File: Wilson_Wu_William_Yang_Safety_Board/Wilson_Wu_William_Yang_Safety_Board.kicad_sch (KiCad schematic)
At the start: 0 parts

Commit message: added can
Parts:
- added J1: 22035035, SMV_Connectors:3pin_CON_22035035_MOL, symbol SMV_Custom:3-pin Mini Molex Spox
- added J2: XT60-M, SMV_Connectors:AMASS_XT60-M, symbol SMV_Custom:XT60-M
- added U1: ~, symbol SMV_Custom:STM32_Nucleo_F446RE
- added U2: MCP2562-E/P, PDIP8_300MC_MCH, symbol can-tranciever:MCP2562-E_P

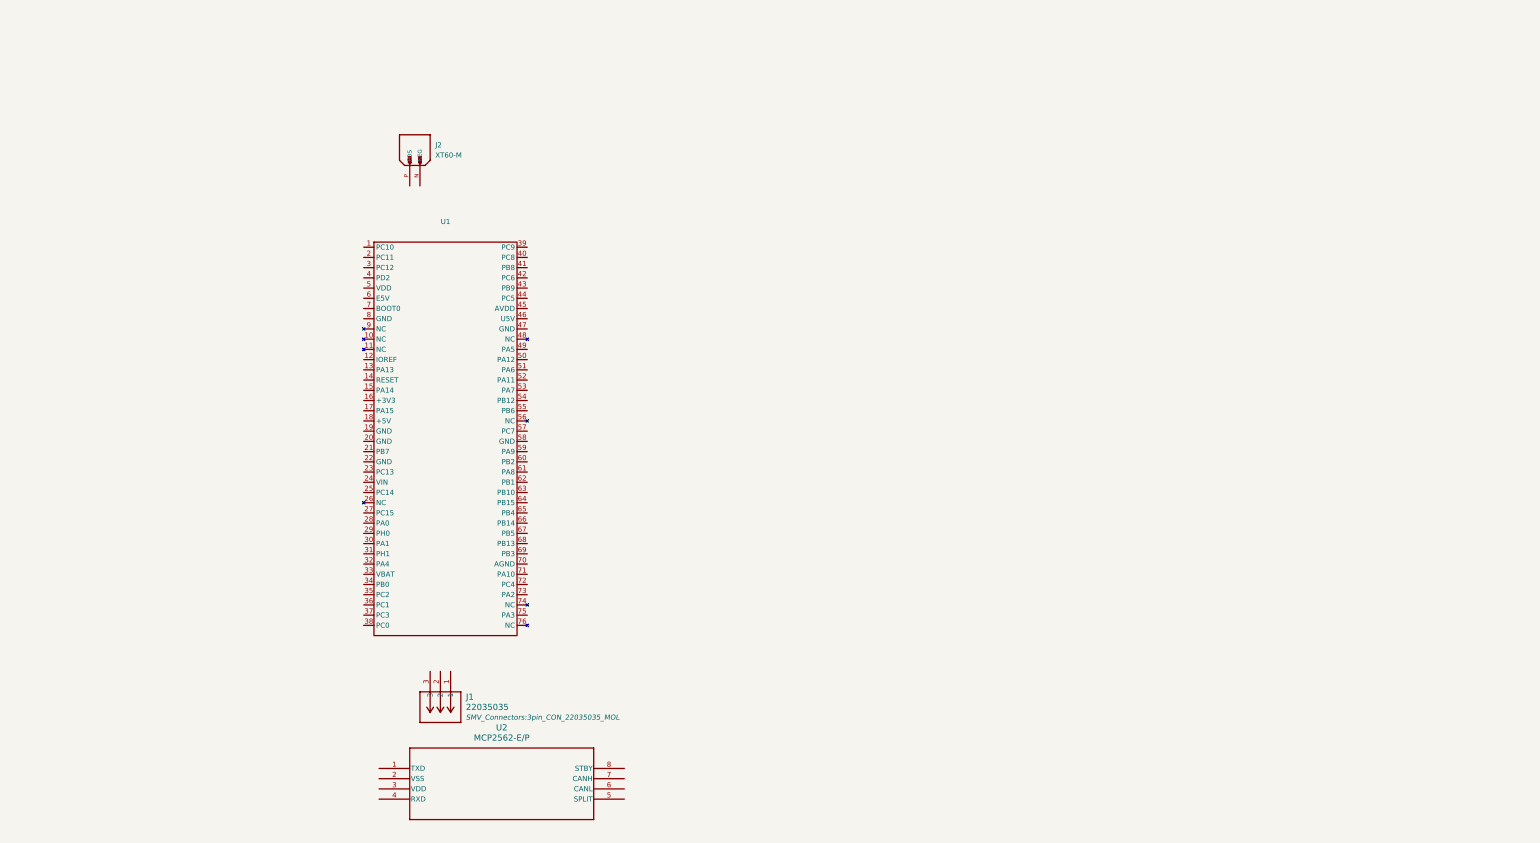
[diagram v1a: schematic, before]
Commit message: added can and power out stuff
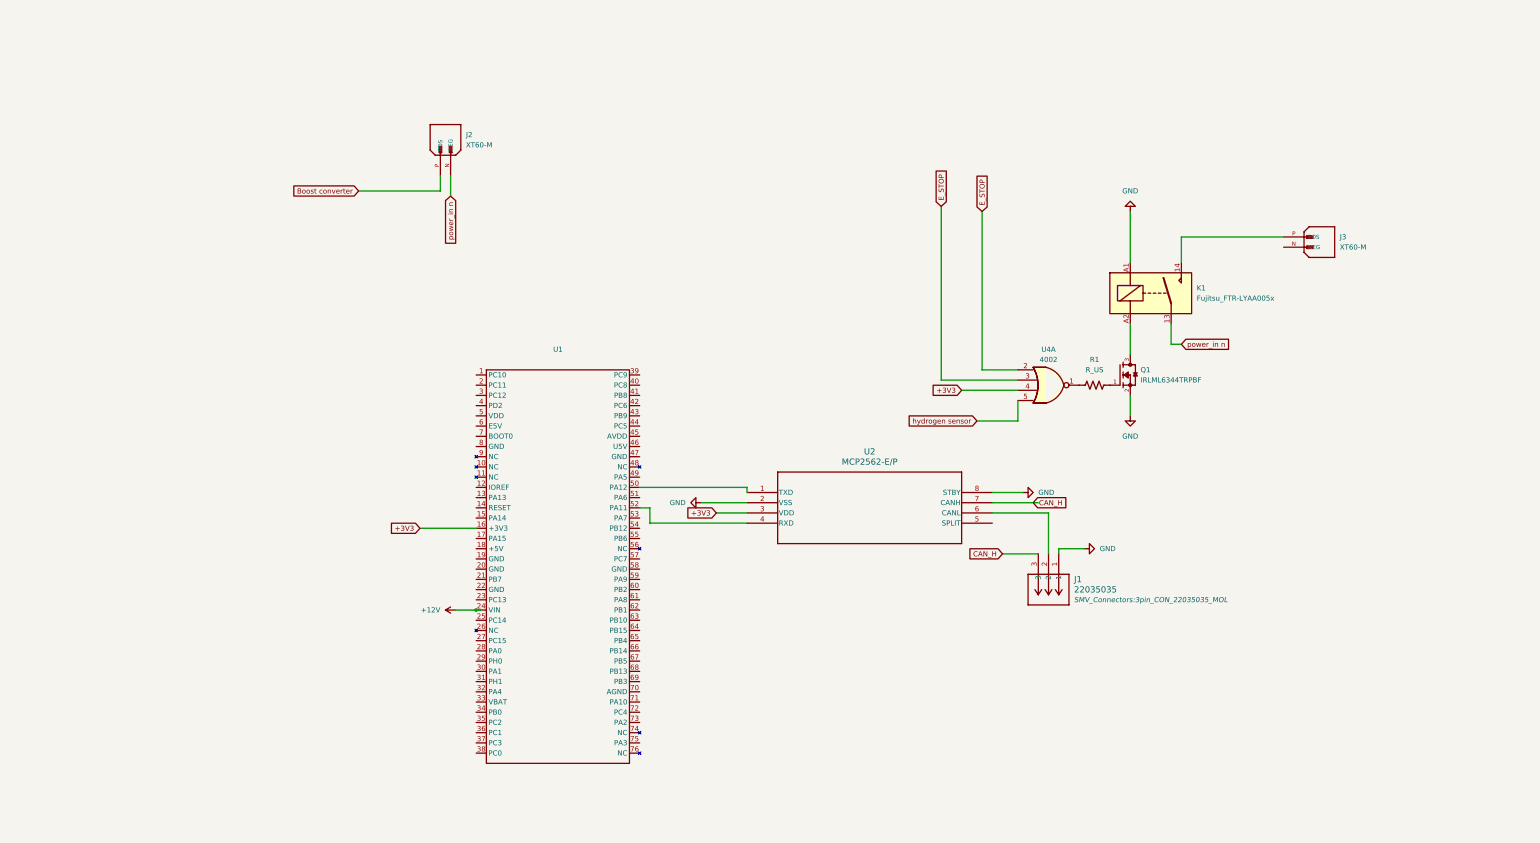
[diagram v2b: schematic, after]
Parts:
- added J3: XT60-M, SMV_Connectors:AMASS_XT60-M, symbol SMV_Custom:XT60-M
- added K1: Fujitsu_FTR-LYAA005x, Relay_THT:Relay_SPST-NO_Fujitsu_FTR-LYAA005x_FormA_Vertical, symbol Relay:Fujitsu_FTR-LYAA005x
- added Q1: IRLML6344TRPBF, IRLML6344TRPBF:TRANS_IRLML6344TRPBF, symbol IRLML6344TRPBF:IRLML6344TRPBF
- added R1: R_US, symbol Device:R_US
- added U4: 4002, symbol 4xxx:4002
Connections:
- net at U2.1 (TXD): now also U1.50 (PA12)
- net GND: now reaches U2.2 (VSS)
- net GND: now also J1.1, U2.8 (STBY), K1.A1, Q1.2
- net +3V3: now reaches U2.3 (VDD)
- net +3V3: now also U1.16 (+3V3), U4.4
- net at U2.4 (RXD): now also U1.52 (PA11)
- net at U2.6 (CANL): now also J1.2
- net CAN_H: now reaches U2.7 (CANH)
- net CAN_H: now also J1.3
- net +12V: now reaches U1.24 (VIN)
- net power_in n: now reaches J2.N (NEG)
- net power_in n: now also K1.13
- net Boost converter: now reaches J2.P (POS)
- new net: J3.P (POS), K1.14
- new net: K1.A2, Q1.3
- new net: R1.1, U4.1
- new net: Q1.1, R1.2
- new net E_STOP: U4.2, U4.3
- new net hydrogen sensor: U4.5
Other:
- moved on the sheet: J1, J2, U1, U2

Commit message: redo
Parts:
- added J4: M22-7130442, M22-7130442_TYC, symbol SMV_Custom:M22-7130442
- added J5: 22035035, SMV_Connectors:3pin_CON_22035035_MOL, symbol SMV_Custom:3-pin Mini Molex Spox
- added J6, J7: 430450200, SMV_Connectors:CONN_SD-43045-001_02_MOL, symbol SMV_Custom:430450200
- added U3: MCP6286T-E/OT, SMV_ICs:SOT-23-5_MC_MCH, symbol SMV_Custom:MCP6286T-E_OT
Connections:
- net GND: now also J5.2, J6.2, J7.2, U3.2 (VSS)
- net at U1.50 (PA12), U2.1 (TXD): now also J4.A1, J4.A4
- net at U1.52 (PA11), U2.4 (RXD): now also J4.A2, J4.A3
- net E_STOP: no longer names the net of U4.2
- net E_STOP: now also J6.1; no longer U4.3
- net hydrogen sensor: no longer names the net of U4.5
- net hydrogen sensor: now also U3.1 (VOUT)
- new net: J7.1, U4.3
- new net +3.3V: J5.1, U3.5 (VDD)
- new net Bridge Circuit: J5.3, U3.3 (VIN+)
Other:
- moved on the sheet: J1, U1, U2

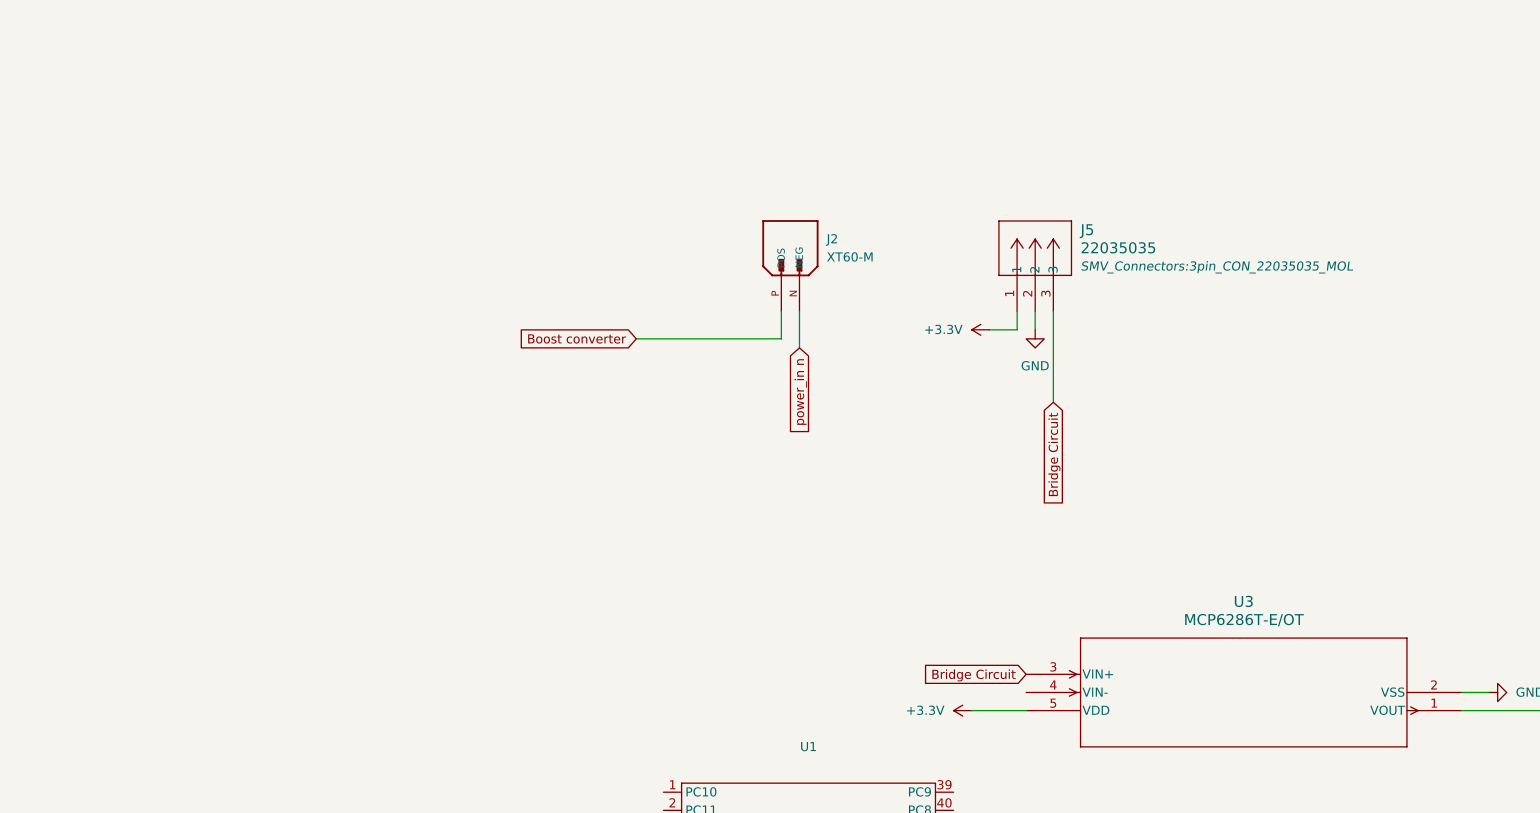
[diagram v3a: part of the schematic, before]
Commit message: added bridge circuit
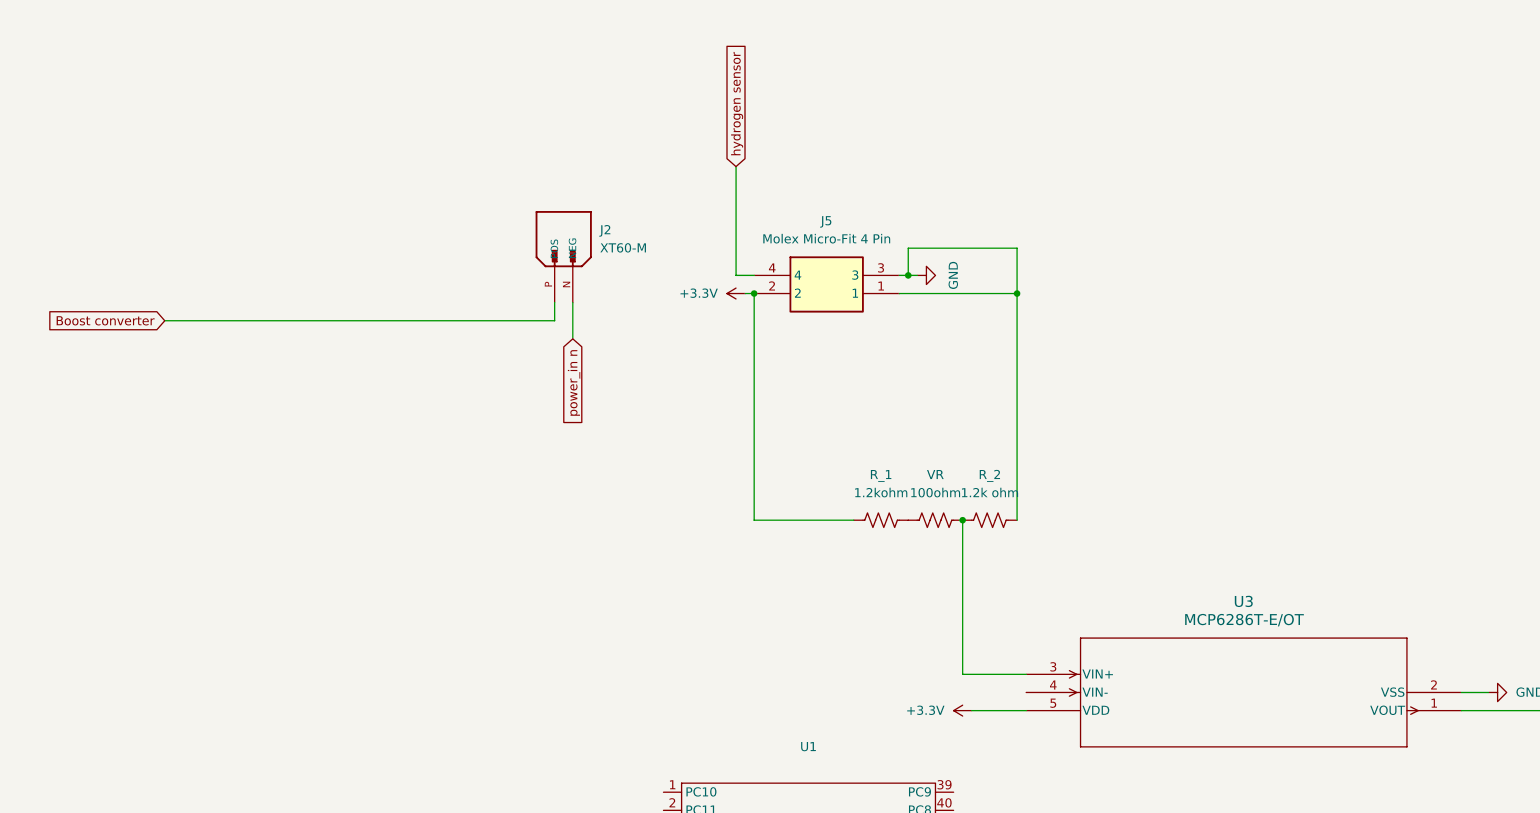
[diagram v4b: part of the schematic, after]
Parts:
- removed J5: 22035035, SMV_Connectors:3pin_CON_22035035_MOL, symbol SMV_Custom:3-pin Mini Molex Spox
- added J5: Molex Micro-Fit 4 Pin, SMV_Connectors:4_pin0430450401, symbol SMV_Custom:Molex Micro-Fit 4 Pin
- added R_1: 1.2kohm, symbol Device:R_US
- added R_2: 1.2k ohm, symbol Device:R_US
- added VR: 100ohm, symbol Device:R_US
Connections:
- net +3.3V: now also J5.2, R_1.1
- net GND: now also J5.1, J5.3, R_2.2
- net Bridge Circuit: no longer names the net of U3.3 (VIN+)
- net Bridge Circuit: now also R_2.1, VR.2
- new net: R_1.2, VR.1
- new net hydrogen sensor: J5.4
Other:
- moved on the sheet: J2

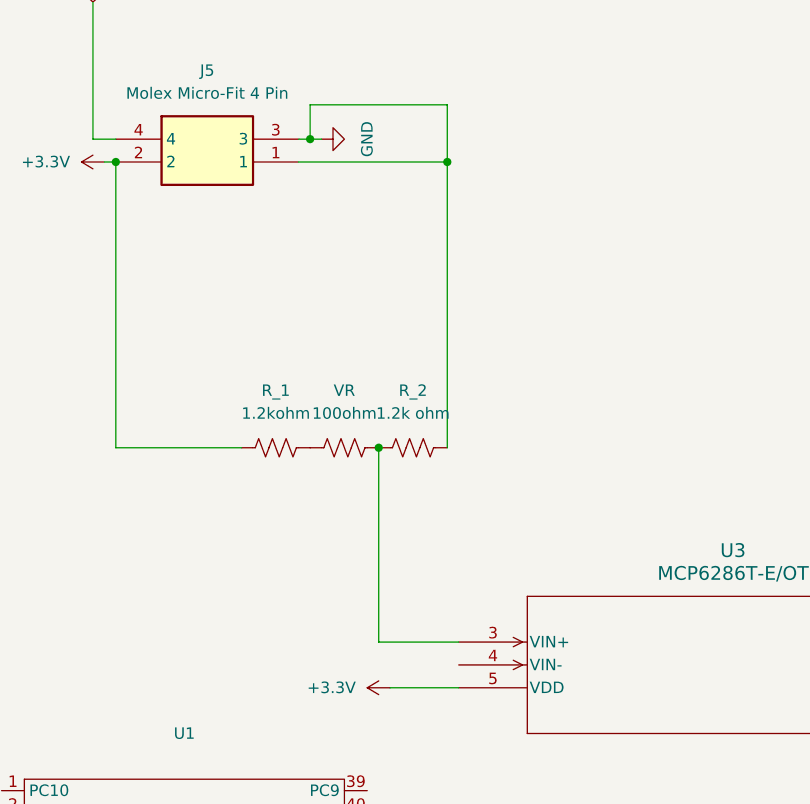
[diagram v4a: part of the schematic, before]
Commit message: edited bridge circuit
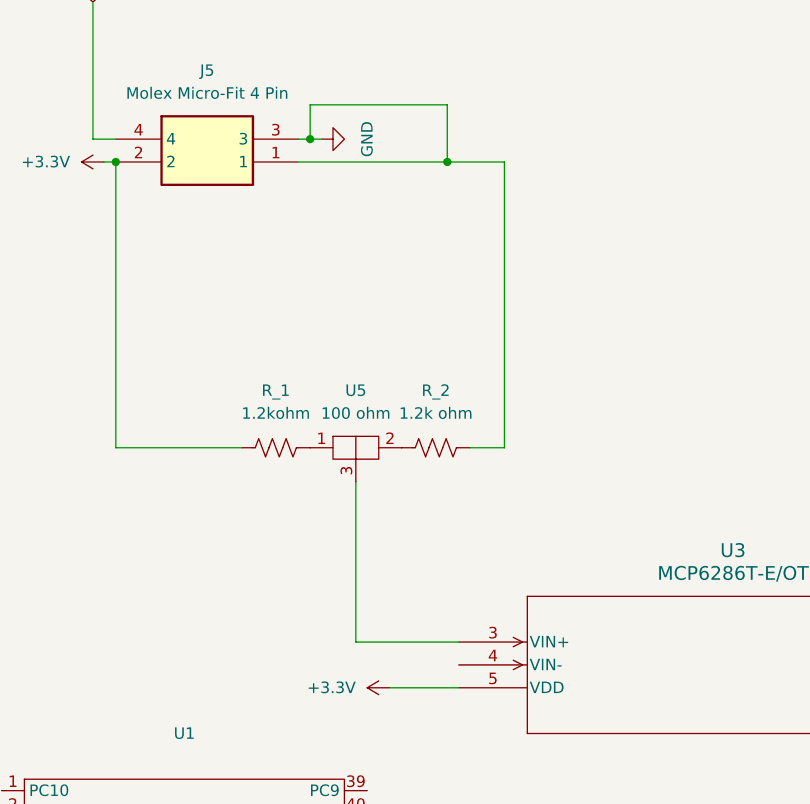
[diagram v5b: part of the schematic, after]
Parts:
- removed VR: 100ohm, symbol Device:R_US
- added U5: 100 ohm, symbol SMV_Custom:Potentiometer_Custom
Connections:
- net at U3.3 (VIN+): now also U5.3; no longer R_2.1
- net at R_1.2: now also U5.1
- new net: R_2.1, U5.2
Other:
- moved on the sheet: R_2
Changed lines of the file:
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@@
-	)
-	(junction
-		(at 78.74 57.15)
-		(diameter 0)
-		(color 0 0 0 0)
 	)
 	(junction
@@
 	(wire
 		(pts
-			(xy 78.74 57.15) (xy 78.74 78.74)
-		)
-		(stroke
-			(width 0)
-			(type default)
-		)
-	)
-	(wire
-		(pts
 			(xy 234.95 64.77) (xy 234.95 69.85)
 		)
@@
 	(wire
 		(pts
+			(xy 92.71 57.15) (xy 88.9 57.15)
+		)
+		(stroke
+			(width 0)
+			(type default)
+		)
+	)
+	(wire
+		(pts
+			(xy 76.2 78.74) (xy 87.63 78.74)
+		)
+		(stroke
+			(width 0)
+			(type default)
+		)
+	)
+	(wire
+		(pts
 			(xy 69.85 25.4) (xy 86.36 25.4)
 		)
@@
 	(wire
 		(pts
+			(xy 92.71 25.4) (xy 86.36 25.4)
+		)
+		(stroke
+			(width 0)
+			(type default)
+		)
+	)
+	(wire
+		(pts
+			(xy 76.2 60.96) (xy 76.2 78.74)
+		)
+		(stroke
+			(width 0)
+			(type default)
+		)
+	)
+	(wire
+		(pts
 			(xy 196.85 76.2) (xy 190.5 76.2)
 		)
@@
 	(wire
 		(pts
-			(xy 78.74 78.74) (xy 87.63 78.74)
-		)
-		(stroke
-			(width 0)
-			(type default)
-		)
-	)
-	(wire
-		(pts
 			(xy 83.82 128.27) (xy 83.82 127)
 		)
@@
 	(wire
 		(pts
-			(xy 86.36 57.15) (xy 86.36 25.4)
+			(xy 92.71 57.15) (xy 92.71 25.4)
 		)
 		(stroke
@@
 	(symbol
 		(lib_id "Device:R_US")
-		(at 82.55 57.15 90)
+		(at 85.09 57.15 90)
 		(unit 1)
 		(exclude_from_sim no)
@@
 		(fields_autoplaced yes)
 		(property "Reference" "R_2"
-			(at 82.55 50.8 90)
+			(at 85.09 50.8 90)
 			(effects
 				(font
@@
 		)
 		(property "Value" "1.2k ohm"
-			(at 82.55 53.34 90)
+			(at 85.09 53.34 90)
 			(effects
 				(font
@@
 		)
 		(property "Footprint" ""
-			(at 82.804 56.134 90)
+			(at 85.344 56.134 90)
 			(effects
 				(font
@@
 		)
 		(property "Datasheet" "~"
-			(at 82.55 57.15 0)
+			(at 85.09 57.15 0)
 			(effects
 				(font
@@
 		)
 		(property "Description" "Resistor, US symbol"
-			(at 82.55 57.15 0)
+			(at 85.09 57.15 0)
 			(effects
 				(font
@@
 	)
 	(symbol
-		(lib_id "Device:R_US")
-		(at 74.93 57.15 90)
-		(unit 1)
-		(exclude_from_sim no)
-		(in_bom yes)
-		(on_board yes)
-		(dnp no)
-		(fields_autoplaced yes)
-		(property "Reference" "VR"
-			(at 74.93 50.8 90)
-			(effects
-				(font
-					(size 1.27 1.27)
-				)
-			)
-		)
-		(property "Value" "100ohm"
-			(at 74.93 53.34 90)
-			(effects
-				(font
-					(size 1.27 1.27)
-				)
-			)
-		)
-		(property "Footprint" ""
-			(at 75.184 56.134 90)
-			(effects
-				(font
-					(size 1.27 1.27)
-				)
-				(hide yes)
-			)
-		)
-		(property "Datasheet" "~"
-			(at 74.93 57.15 0)
-			(effects
-				(font
-					(size 1.27 1.27)
-				)
-				(hide yes)
-			)
-		)
-		(property "Description" "Resistor, US symbol"
-			(at 74.93 57.15 0)
-			(effects
-				(font
-					(size 1.27 1.27)
-				)
-				(hide yes)
-			)
-		)
-		(pin "1"
-		)
-		(pin "2"
-		)
-		(instances
-			(project ""
-				(path "/fa857c32-0741-4b91-b122-1a57686bb514"
-					(reference "VR")
-					(unit 1)
-				)
-			)
-		)
-	)
-	(symbol
 		(lib_id "power:+3.3V")
 		(at 48.26 25.4 90)
@@
 					(unit 1)
 				)
+			)
+		)
+	)
+	(symbol
+		(lib_id "SMV_Custom:Potentiometer_Custom")
+		(at 76.2 54.61 0)
+		(unit 1)
+		(exclude_from_sim no)
+		(in_bom yes)
+		(on_board yes)
+		(dnp no)
+		(fields_autoplaced yes)
+		(property "Reference" "U5"
+			(at 76.2 50.8 0)
+			(effects
+				(font
+					(size 1.27 1.27)
+				)
+			)
+		)
+		(property "Value" "100 ohm"
+			(at 76.2 53.34 0)
+			(effects
+				(font
+					(size 1.27 1.27)
+				)
+			)
+		)
+		(property "Footprint" ""
+			(at 76.2 54.61 0)
+			(effects
+				(font
+					(size 1.27 1.27)
+				)
+				(hide yes)
+			)
+		)
+		(property "Datasheet" "https://www.vishay.com/docs/50020/rssd.pdf"
+			(at 76.2 54.61 0)
+			(effects
+				(font
+					(size 1.27 1.27)
+				)
+				(hide yes)
+			)
+		)
+		(property "Description" "100 ohm potentiometer for hydrogen sensor bridge circuit"
+			(at 76.2 54.61 0)
+			(effects
+				(font
+					(size 1.27 1.27)
+				)
+				(hide yes)
+			)
+		)
+		(pin "3"
+		)
+		(pin "1"
+		)
+		(pin "2"
+		)
+		(instances
+			(project ""
+				(path "/fa857c32-0741-4b91-b122-1a57686bb514"
+					(reference "U5")
+					(unit 1)
+				)
